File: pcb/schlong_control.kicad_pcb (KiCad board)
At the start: 2 copper layers, 88.9 x 95.2 mm, 38 parts, among them P1 Power Connector (120V AC), P2 Input, P3 Output, U1 74HC595, U2 MOC3063M, U3 MOC3063M, U4 MOC3063M, U5 MOC3063M, U6 MOC3063M, U7 LM7805

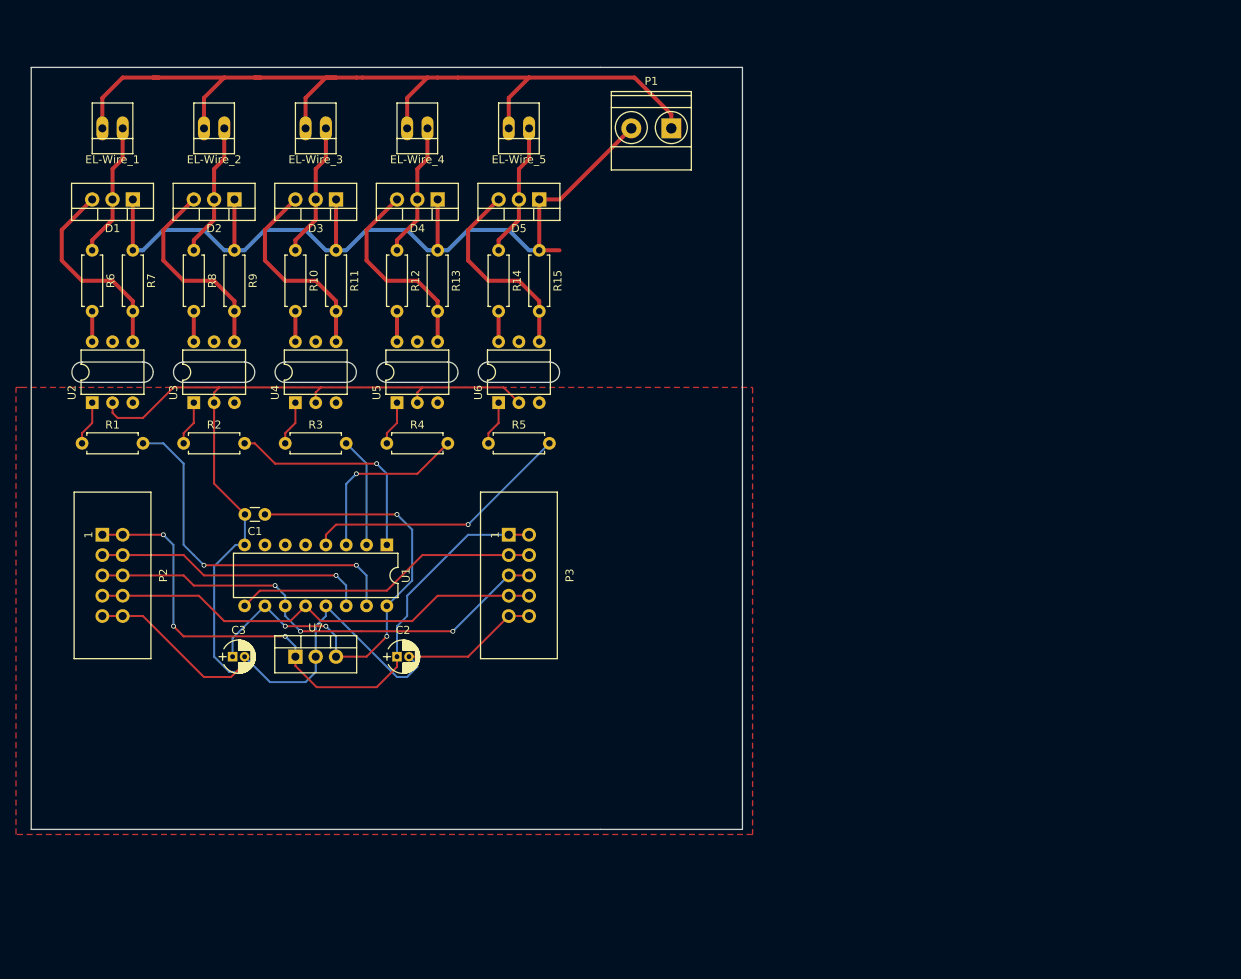
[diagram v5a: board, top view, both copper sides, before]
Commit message: pcb: shrinkify board
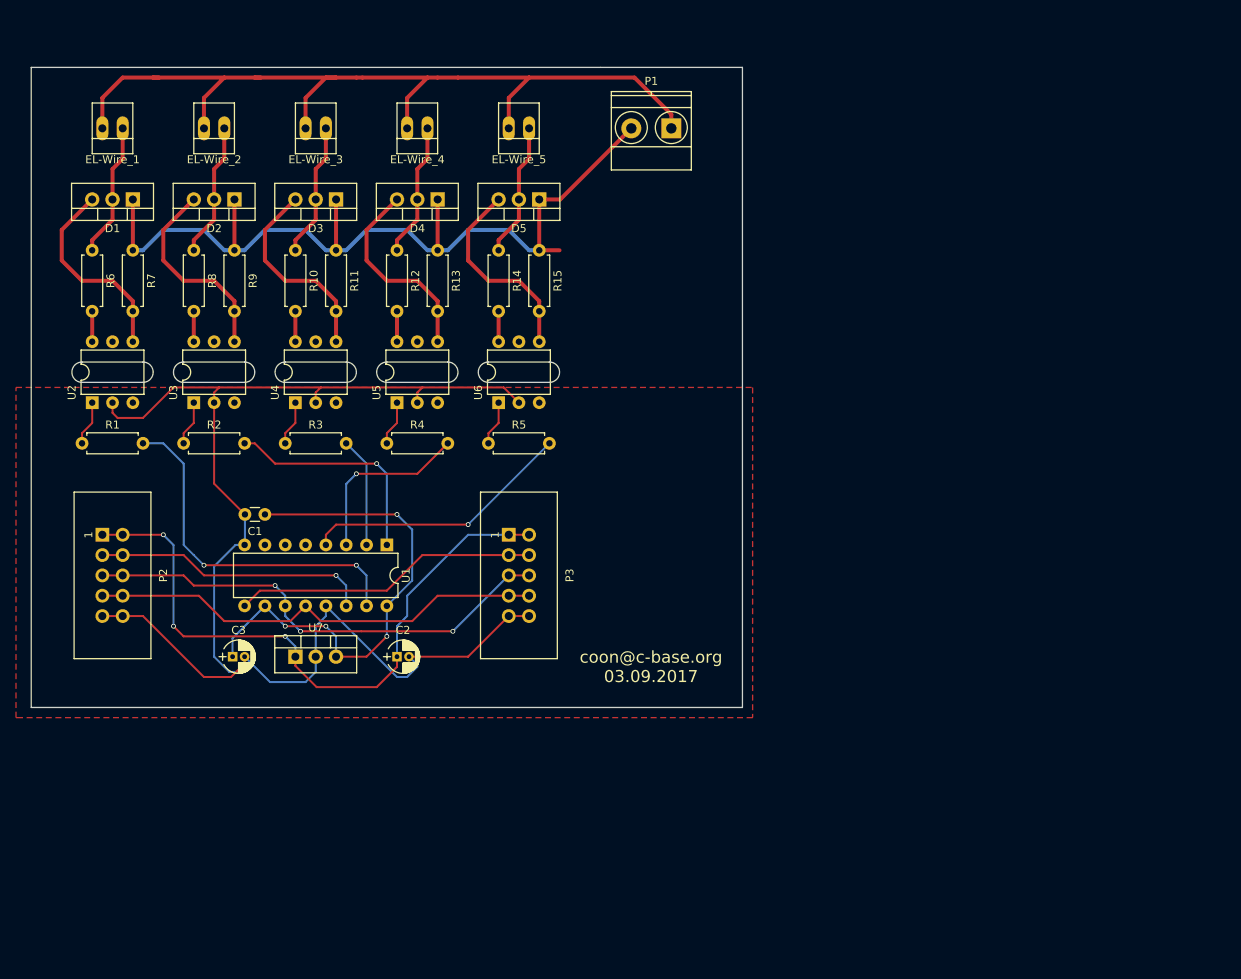
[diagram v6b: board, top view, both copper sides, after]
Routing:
- net (no net): track 0.00 -> 168.9 mm
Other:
- board size 88.9 x 95.2 mm -> 88.9 x 80 mm
- board text added: "coon@c-base.org 03.09.2017"
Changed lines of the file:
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@@
     (links 85)
     (no_connects 0)
-    (area 50.724999 25.324999 139.775001 120.725001)
+    (area 50.724999 25.324999 139.775001 105.485001)
     (thickness 1.6)
     (drawings 28)
-    (tracks 295)
+    (tracks 297)
     (zones 0)
     (modules 38)
@@
   )
   (setup
-    (last_trace_width 0.5)
+    (last_trace_width 0.25)
     (user_trace_width 0.5)
     (user_trace_width 0.75)
@@
     )
   )
+  (gr_line (start 50.8 105.41) (end 50.8 25.4) (layer Edge.Cuts) (width 0.15))
+  (gr_line (start 139.7 25.4) (end 139.7 105.41) (layer Edge.Cuts) (width 0.15))
+  (gr_line (start 50.8 105.41) (end 139.7 105.41) (layer Edge.Cuts) (width 0.15))
+  (gr_text "coon@c-base.org\n03.09.2017" (at 128.27 100.33) (layer F.SilkS)
+    (effects (font (size 1.5 1.5) (thickness 0.3)))
+  )
   (dimension 95.25 (width 0.3) (layer Eco1.User)
     (gr_text "95,250 mm" (at 147.4 73.025 270) (layer Eco1.User)
@@
   )
   (gr_line (start 139.7 25.4) (end 121.92 25.4) (layer Edge.Cuts) (width 0.15))
-  (gr_line (start 139.7 120.65) (end 139.7 25.4) (layer Edge.Cuts) (width 0.15))
-  (gr_line (start 121.92 120.65) (end 139.7 120.65) (layer Edge.Cuts) (width 0.15))
   (gr_arc (start 115.57 63.5) (end 115.57 62.23) (angle 180) (layer Edge.Cuts) (width 0.15))
   (gr_line (start 107.95 64.77) (end 115.57 64.77) (layer Edge.Cuts) (width 0.15))
@@
   (gr_line (start 57.15 64.77) (end 64.77 64.77) (layer Edge.Cuts) (width 0.15))
   (gr_line (start 57.15 62.23) (end 64.77 62.23) (layer Edge.Cuts) (width 0.15))
-  (gr_line (start 50.8 25.4) (end 50.8 120.65) (angle 90) (layer Edge.Cuts) (width 0.15))
-  (gr_line (start 50.8 120.65) (end 121.92 120.65) (angle 90) (layer Edge.Cuts) (width 0.15))
   (gr_line (start 121.92 25.4) (end 50.8 25.4) (angle 90) (layer Edge.Cuts) (width 0.15))
+  (segment (start 139.7 25.4) (end 139.7 105.41) (width 0.25) (layer Dwgs.User) (net 0))
+  (segment (start 50.8 106.68) (end 139.7 106.68) (width 0.25) (layer Dwgs.User) (net 0))
   (segment (start 75.97 99.06) (end 75.97 96.75) (width 0.25) (layer B.Cu) (net 1))
   (segment (start 96.52 81.28) (end 98.425 83.185) (width 0.25) (layer B.Cu) (net 1))
@@
     (polygon
       (pts
-        (xy 49.53 65.405) (xy 140.97 65.405) (xy 140.97 121.285) (xy 48.895 121.285) (xy 48.895 65.405)
+        (xy 48.895 65.405) (xy 140.97 65.405) (xy 140.97 106.68) (xy 49.53 106.68) (xy 48.895 106.68)
       )
     )

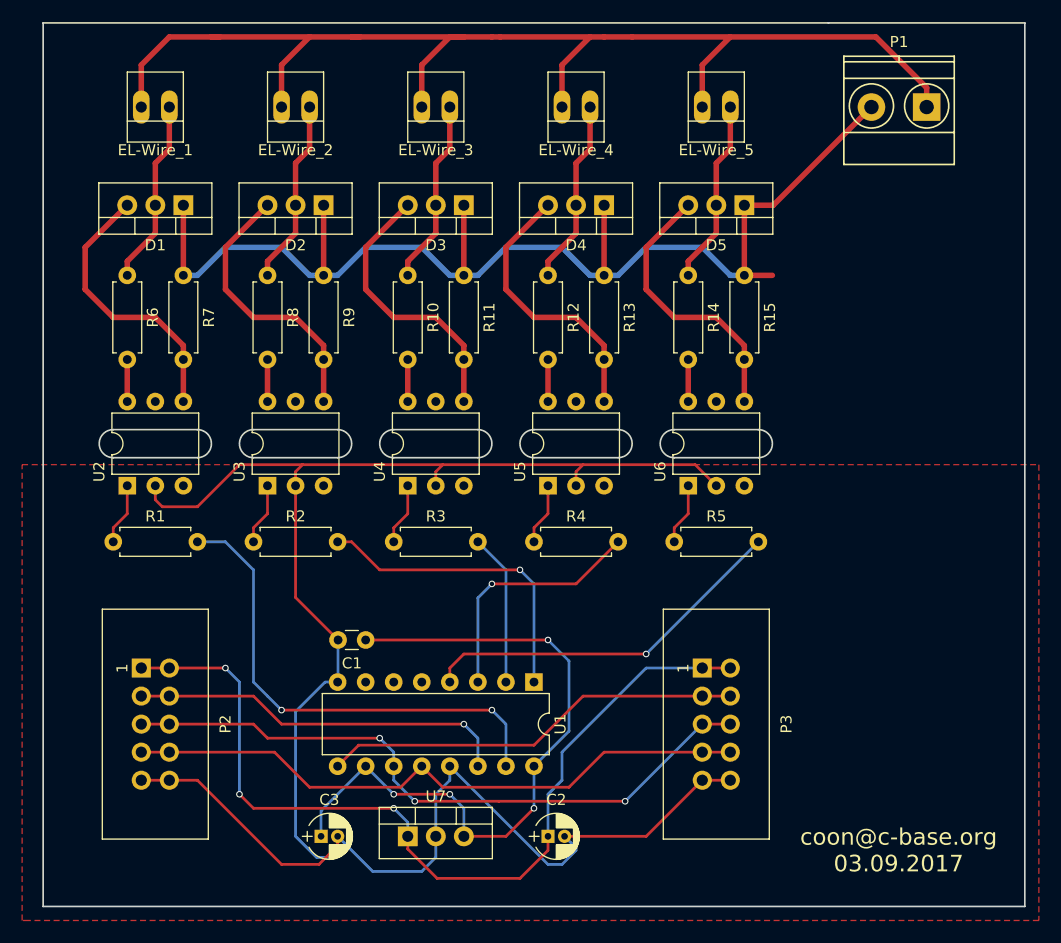
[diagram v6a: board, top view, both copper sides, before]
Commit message: pcb: add mounting holes
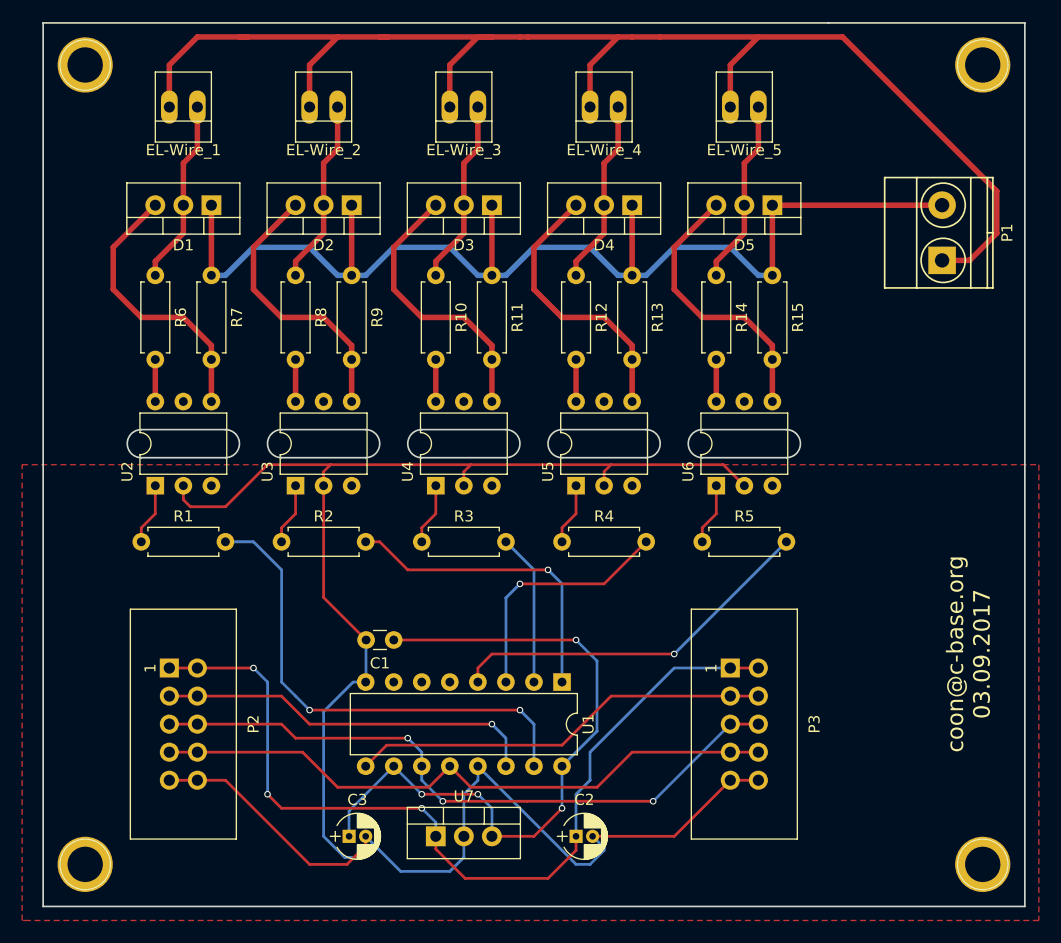
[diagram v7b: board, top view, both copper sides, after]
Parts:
- added REF**: 1pin, Connectors:1pin, F.Cu at (135.9, 101.6)
- added REF**: 1pin, Connectors:1pin, F.Cu at (54.6, 101.6)
- added REF**: 1pin, Connectors:1pin, F.Cu at (135.9, 29.2)
- added REF**: 1pin, Connectors:1pin, F.Cu at (54.6, 29.2)
- moved P1 14.0 mm to (132.2, 46.9), turned to 90 degrees
- moved C2 2.54 mm to (99.1, 99.1)
- moved C3 2.54 mm to (78.5, 99.1)
- moved D1 2.54 mm to (66.0, 41.9)
- moved D4 2.54 mm to (104.1, 41.9)
- moved D5 2.54 mm to (116.8, 41.9)
- moved EL-Wire_3 2.54 mm to (90.2, 33.0)
- moved EL-Wire_4 2.54 mm to (102.9, 33.0)
- moved P3 2.54 mm to (113.0, 83.8)
- moved R10 2.54 mm to (86.4, 48.3)
- moved R12 2.54 mm to (99.1, 48.3)
- moved R13 2.54 mm to (104.1, 48.3)
- moved R14 2.54 mm to (111.8, 48.3)
- moved R15 2.54 mm to (116.8, 48.3)
- moved R2 2.54 mm to (72.4, 72.4)
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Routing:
- net /AC_P: track 115.0 -> 130.7 mm
- net /AC_N: track 108.7 -> 106.3 mm
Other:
- outline, holes or cut-outs redrawn

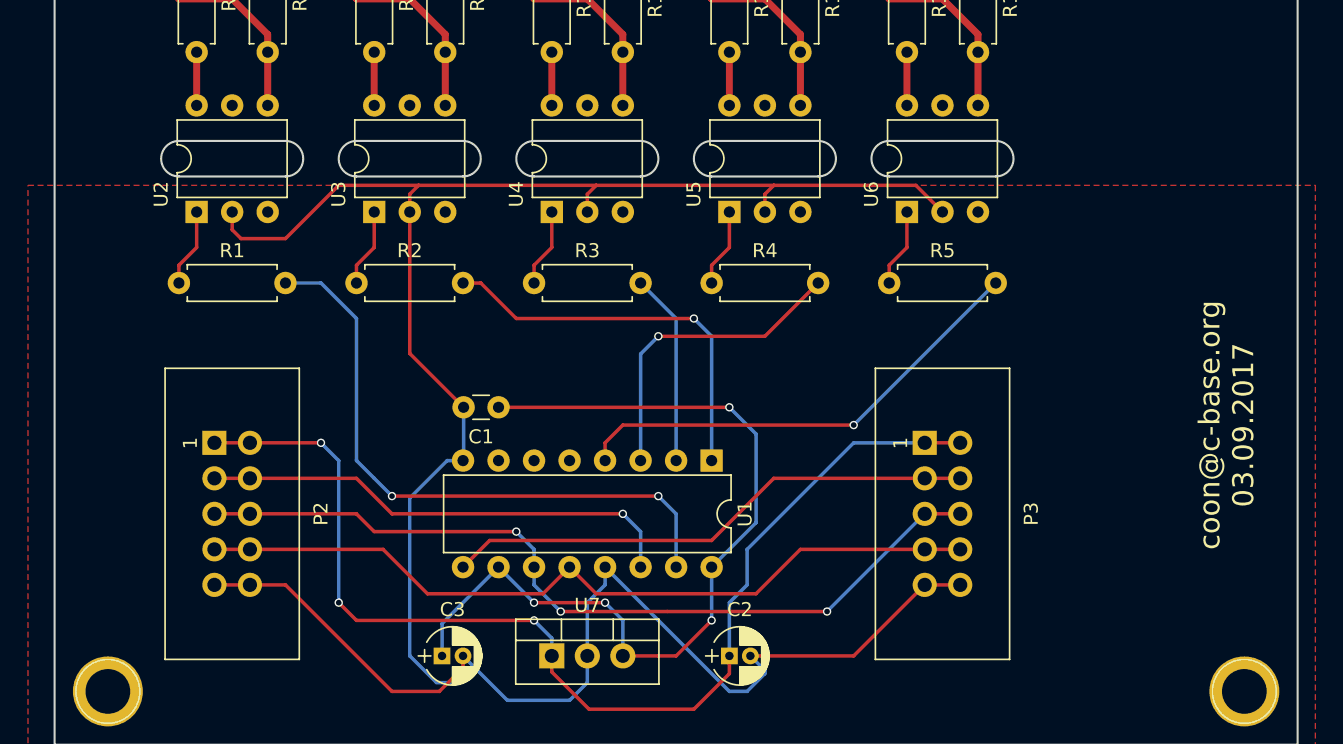
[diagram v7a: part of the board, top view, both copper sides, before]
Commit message: pcb: adjust footprints of IDC headers
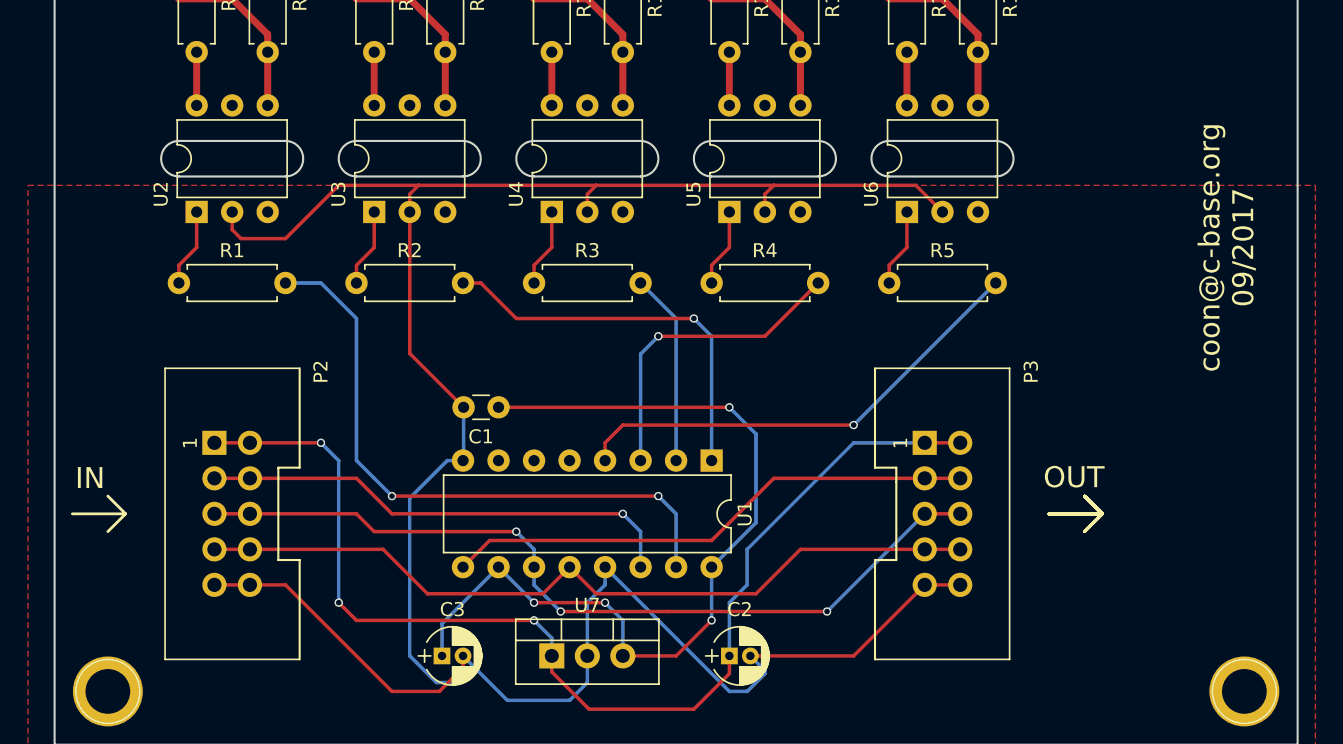
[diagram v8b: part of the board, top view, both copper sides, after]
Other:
- board text added: "IN"
- board text added: "OUT"
- board text added: "coon@c-base.org 09/2017"
- board text removed: "coon@c-base.org 03.09.2017"
